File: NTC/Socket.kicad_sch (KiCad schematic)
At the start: 3 parts, among them X1 Conn_01x06_Pin, X2 Conn_01x06_Pin

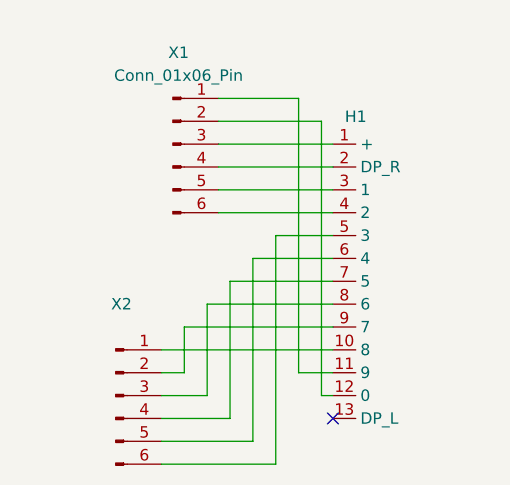
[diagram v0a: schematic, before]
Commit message: Changed to 14pin socket
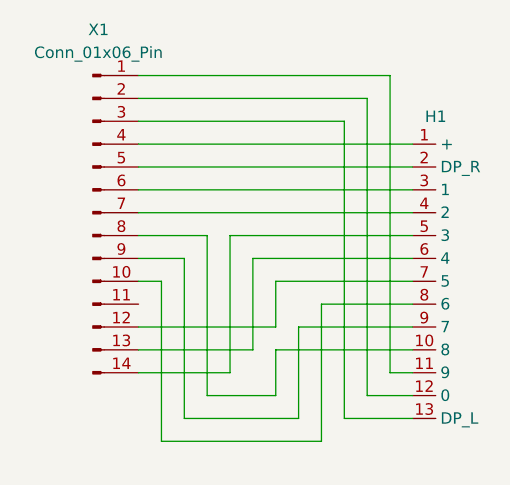
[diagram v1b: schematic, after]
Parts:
- removed X2: Conn_01x06_Pin, Nixie:Pinbar_1-6-m-b, symbol Connector:Conn_01x06_Pin
- X1: footprint Nixie:Pinbar_1-6-m-a -> Nixie:Pinbar_4-14-m; symbol Connector:Conn_01x06_Pin -> Connector:Conn_01x14_Pin
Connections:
- net at H1.1 (+): now also X1.4 (Pin_4); no longer X1.3 (Pin_3)
- net at H1.10 (8): now also X1.8 (Pin_8)
- net at H1.13 (DP_L): now also X1.3 (Pin_3)
- net at H1.2 (DP_R): now also X1.5 (Pin_5); no longer X1.4 (Pin_4)
- net at H1.3 (1): now also X1.6 (Pin_6); no longer X1.5 (Pin_5)
- net at H1.4 (2): now also X1.7 (Pin_7); no longer X1.6 (Pin_6)
- net at H1.5 (3): now also X1.14 (Pin_14)
- net at H1.6 (4): now also X1.13 (Pin_13)
- net at H1.7 (5): now also X1.12 (Pin_12)
- net at H1.8 (6): now also X1.10 (Pin_10)
- net at H1.9 (7): now also X1.9 (Pin_9)
- no-connect marks 1 -> 0
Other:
- moved on the sheet: H1
